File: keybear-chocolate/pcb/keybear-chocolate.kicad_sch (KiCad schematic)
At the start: 95 parts, among them J1 MJ-4PP-9, J2 BATT, J3 LED, J4 OLED, SW1 SW_PUSH, SW10 SW_PUSH, SW11 SW_PUSH, SW12 SW_PUSH, SW13 SW_PUSH, SW14 SW_PUSH, SW15 SW_PUSH, SW16 SW_PUSH, SW17 SW_PUSH, SW18 SW_PUSH, SW19 SW_PUSH, SW2 SW_PUSH, SW20 SW_PUSH, SW21 SW_PUSH, SW22 SW_PUSH, SW23 SW_PUSH, SW25 Rotary_Encoder_Switch, SW3 SW_PUSH, SW30 BATT_SW, SW4 SW_PUSH, SW5 SW_PUSH, SW6 SW_PUSH, SW7 SW_PUSH, SW8 SW_PUSH, SW9 SW_PUSH, U1 ProMicro

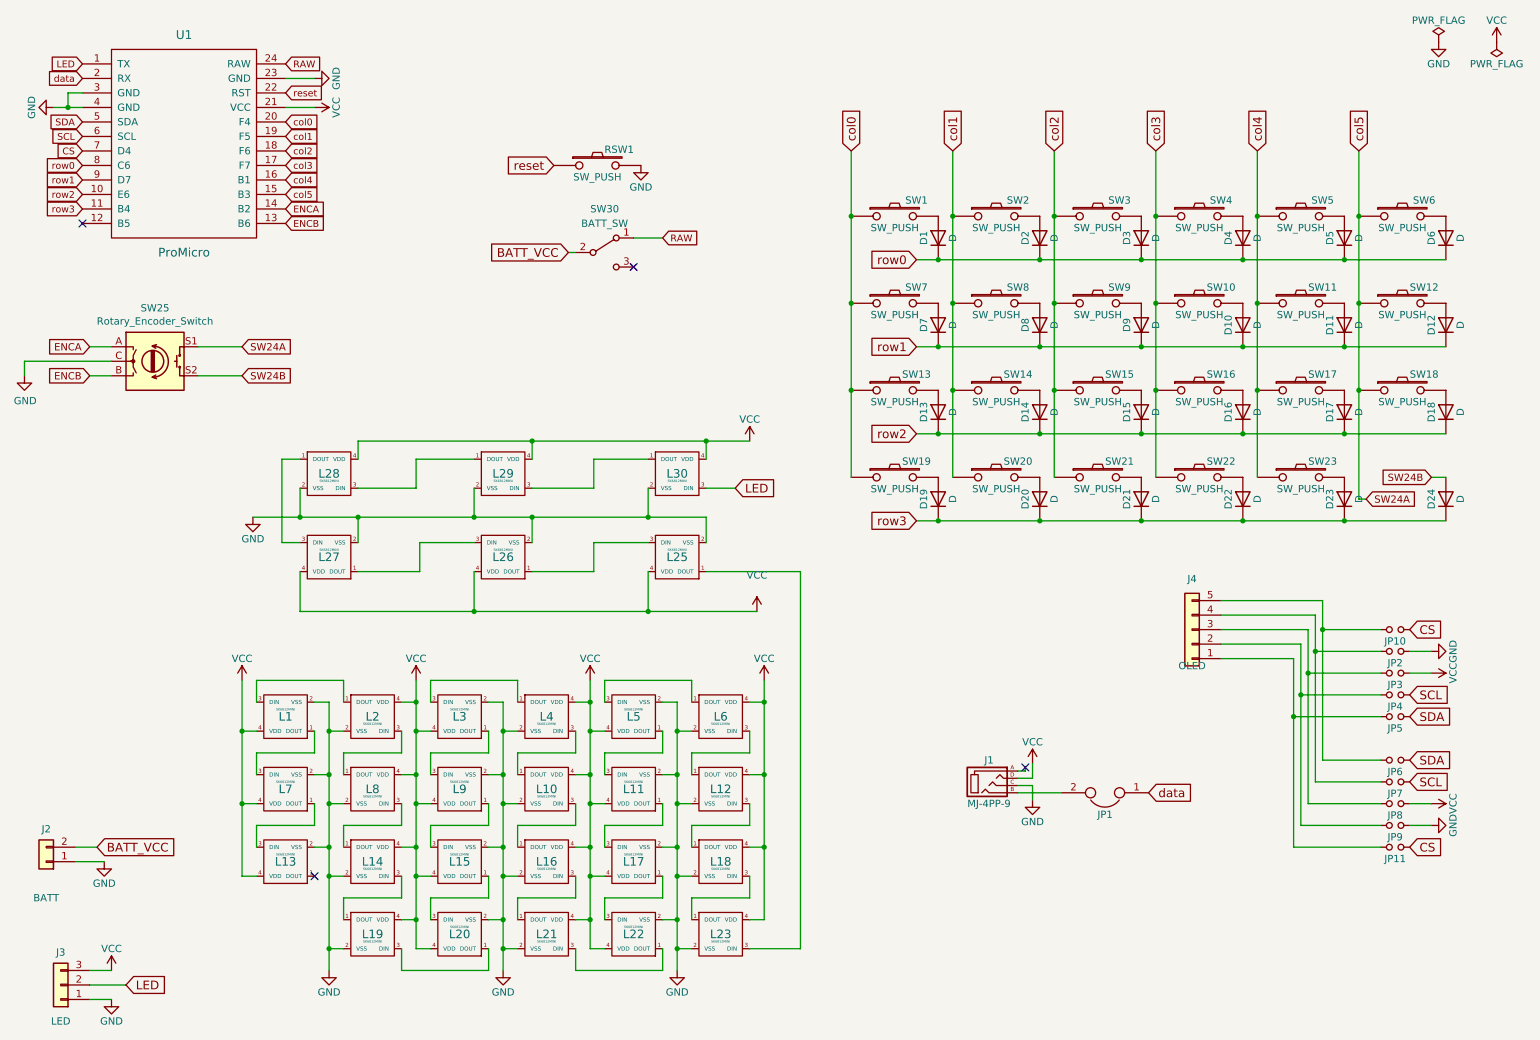
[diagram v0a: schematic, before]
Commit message: batt strip connection updated. tracks made
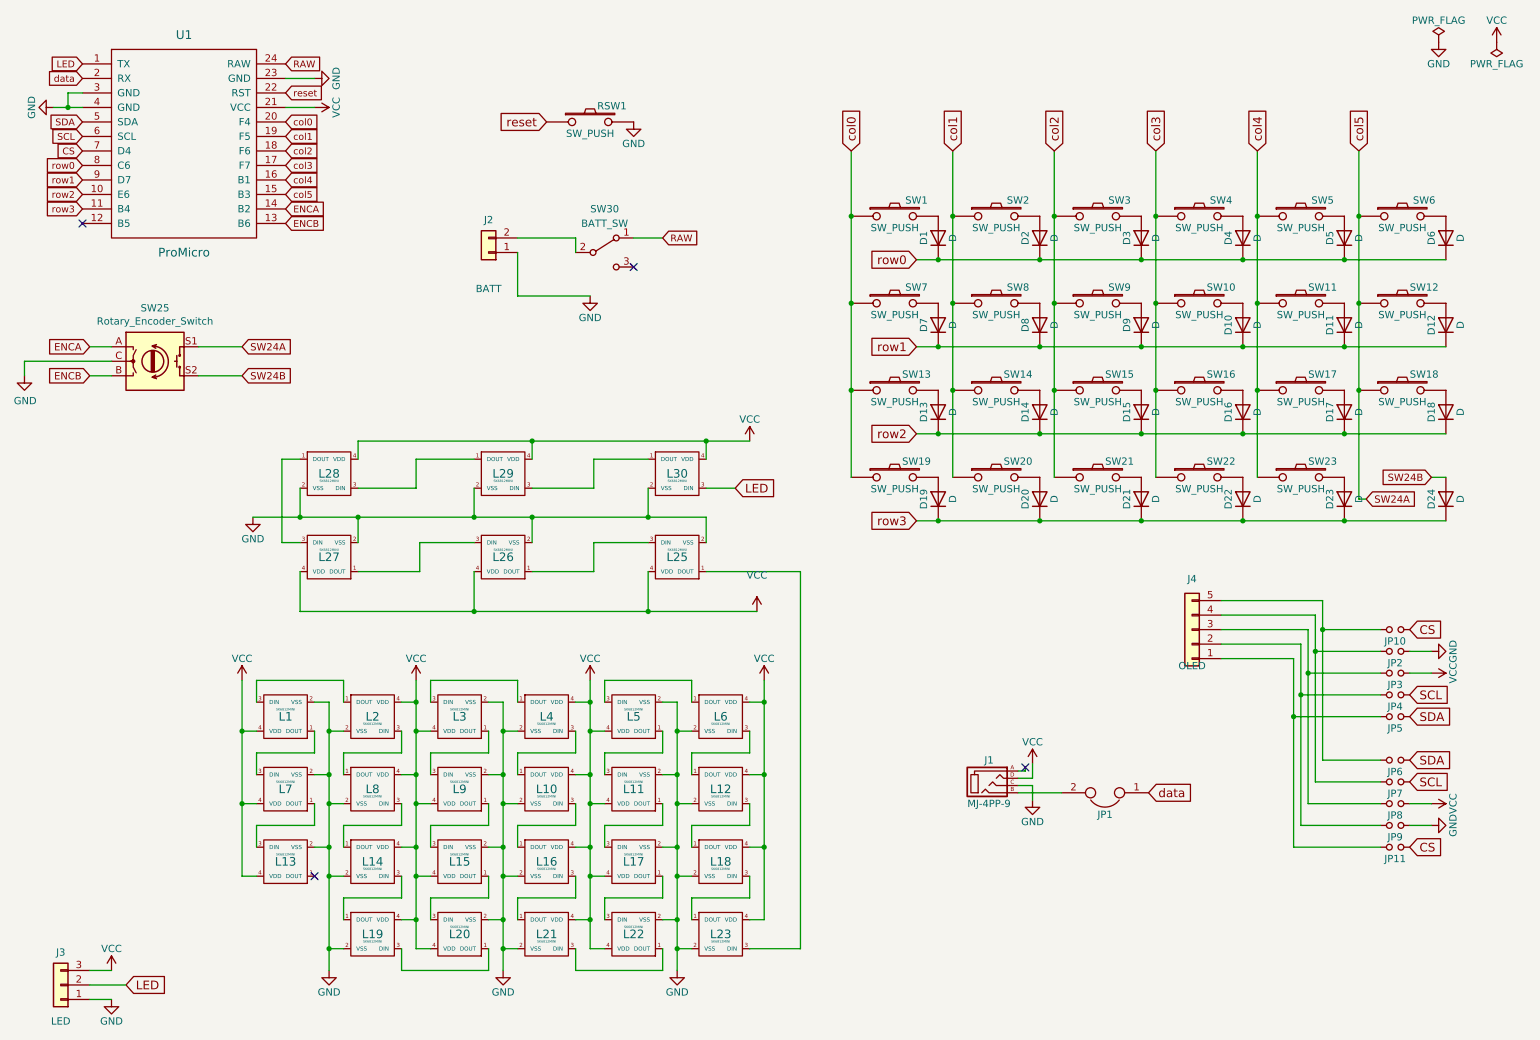
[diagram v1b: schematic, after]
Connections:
- net BATT_VCC: no longer names the net of J2.2 (Pin_2), SW30.2 (B)
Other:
- moved on the sheet: J2, RSW1
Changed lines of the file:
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@@
     (stroke (width 0) (type default))
   )
-  (wire (pts (xy 27.94 163.83) (xy 33.02 163.83))
+  (wire (pts (xy 105.41 54.61) (xy 115.57 54.61))
     (stroke (width 0) (type default))
   )
@@
     (stroke (width 0) (type default))
   )
+  (wire (pts (xy 105.41 64.77) (xy 118.11 64.77))
+    (stroke (width 0) (type default))
+  )
   (wire (pts (xy 115.57 161.29) (xy 118.11 161.29))
     (stroke (width 0) (type default))
@@
     (stroke (width 0) (type default))
   )
+  (wire (pts (xy 115.57 54.61) (xy 115.57 57.15))
+    (stroke (width 0) (type default))
+  )
   (wire (pts (xy 234.95 66.04) (xy 234.95 81.28))
     (stroke (width 0) (type default))
@@
     (stroke (width 0) (type default))
   )
-  (wire (pts (xy 31.75 161.29) (xy 27.94 161.29))
-    (stroke (width 0) (type default))
-  )
   (wire (pts (xy 130.81 179.07) (xy 130.81 182.88))
     (stroke (width 0) (type default))
@@
     (stroke (width 0) (type default))
   )
+  (wire (pts (xy 105.41 57.15) (xy 105.41 64.77))
+    (stroke (width 0) (type default))
+  )
   (wire (pts (xy 146.05 148.59) (xy 148.59 148.59))
     (stroke (width 0) (type default))
@@
     (stroke (width 0) (type default))
   )
-  (wire (pts (xy 115.57 57.15) (xy 114.3 57.15))
-    (stroke (width 0) (type default))
-  )
   (wire (pts (xy 243.84 153.67) (xy 256.54 153.67))
     (stroke (width 0) (type default))
@@
     )
   )
-  (global_label "BATT_VCC" (shape input) (at 114.3 57.15 180) (fields_autoplaced)
-    (effects (font (size 1.524 1.524)) (justify right))
-    (property "Intersheetrefs" "${INTERSHEET_REFS}" (at 100.8353 57.15 0)
-      (effects (font (size 1.27 1.27)) (justify right) hide)
-    )
-  )
   (global_label "SDA" (shape input) (at 261.62 146.05 0) (fields_autoplaced)
     (effects (font (size 1.524 1.524)) (justify left))
@@
     )
   )
-  (global_label "reset" (shape input) (at 111.76 41.91 180) (fields_autoplaced)
+  (global_label "reset" (shape input) (at 110.49 34.29 180) (fields_autoplaced)
     (effects (font (size 1.524 1.524)) (justify right))
-    (property "Intersheetrefs" "${INTERSHEET_REFS}" (at 103.3026 41.91 0)
+    (property "Intersheetrefs" "${INTERSHEET_REFS}" (at 102.0326 34.29 0)
       (effects (font (size 1.27 1.27)) (justify right) hide)
     )
@@
     )
   )
-  (global_label "BATT_VCC" (shape input) (at 31.75 161.29 0) (fields_autoplaced)
-    (effects (font (size 1.524 1.524)) (justify left))
-    (property "Intersheetrefs" "${INTERSHEET_REFS}" (at 45.2147 161.29 0)
-      (effects (font (size 1.27 1.27)) (justify left) hide)
-    )
-  )
   (global_label "col2" (shape input) (at 64.77 39.37 0) (fields_autoplaced)
     (effects (font (size 1.1938 1.1938)) (justify left))
@@
     )
   )
-  (symbol (lib_id "corne-chocolate-rescue:SW_PUSH-kbd") (at 119.38 41.91 0) (unit 1)
+  (symbol (lib_id "corne-chocolate-rescue:SW_PUSH-kbd") (at 118.11 34.29 0) (unit 1)
     (in_bom yes) (on_board yes) (dnp no)
-    (property "Reference" "RSW1" (at 123.19 39.116 0)
+    (property "Reference" "RSW1" (at 121.92 31.496 0)
       (effects (font (size 1.27 1.27)))
     )
-    (property "Value" "SW_PUSH" (at 119.38 43.942 0)
+    (property "Value" "SW_PUSH" (at 118.11 36.322 0)
       (effects (font (size 1.27 1.27)))
     )
-    (property "Footprint" "kbd:ResetSW" (at 119.38 41.91 0)
+    (property "Footprint" "kbd:ResetSW" (at 118.11 34.29 0)
       (effects (font (size 1.27 1.27)) hide)
     )
-    (property "Datasheet" "" (at 119.38 41.91 0)
+    (property "Datasheet" "" (at 118.11 34.29 0)
       (effects (font (size 1.27 1.27)))
     )
@@
     )
   )
-  (symbol (lib_id "power:GND") (at 127 41.91 0) (unit 1)
+  (symbol (lib_id "power:GND") (at 125.73 34.29 0) (unit 1)
     (in_bom yes) (on_board yes) (dnp no)
-    (property "Reference" "#PWR07" (at 127 48.26 0)
+    (property "Reference" "#PWR07" (at 125.73 40.64 0)
       (effects (font (size 1.27 1.27)) hide)
     )
-    (property "Value" "GND" (at 127 45.72 0)
+    (property "Value" "GND" (at 125.73 38.1 0)
       (effects (font (size 1.27 1.27)))
     )
-    (property "Footprint" "" (at 127 41.91 0)
+    (property "Footprint" "" (at 125.73 34.29 0)
       (effects (font (size 1.27 1.27)) hide)
     )
-    (property "Datasheet" "" (at 127 41.91 0)
+    (property "Datasheet" "" (at 125.73 34.29 0)
       (effects (font (size 1.27 1.27)) hide)
     )
@@
     )
   )
-  (symbol (lib_id "power:GND") (at 33.02 163.83 0) (unit 1)
+  (symbol (lib_id "power:GND") (at 118.11 64.77 0) (unit 1)
     (in_bom yes) (on_board yes) (dnp no)
-    (property "Reference" "#PWR021" (at 33.02 170.18 0)
+    (property "Reference" "#PWR021" (at 118.11 71.12 0)
       (effects (font (size 1.27 1.27)) hide)
     )
-    (property "Value" "GND" (at 33.02 167.64 0)
+    (property "Value" "GND" (at 118.11 68.58 0)
       (effects (font (size 1.27 1.27)))
     )
-    (property "Footprint" "" (at 33.02 163.83 0)
+    (property "Footprint" "" (at 118.11 64.77 0)
       (effects (font (size 1.27 1.27)) hide)
     )
-    (property "Datasheet" "" (at 33.02 163.83 0)
+    (property "Datasheet" "" (at 118.11 64.77 0)
       (effects (font (size 1.27 1.27)) hide)
     )
@@
     )
   )
-  (symbol (lib_id "Connector_Generic:Conn_01x02") (at 22.86 163.83 180) (unit 1)
+  (symbol (lib_id "Connector_Generic:Conn_01x02") (at 100.33 57.15 180) (unit 1)
     (in_bom yes) (on_board yes) (dnp no)
-    (property "Reference" "J2" (at 22.86 158.115 0)
+    (property "Reference" "J2" (at 100.33 51.435 0)
       (effects (font (size 1.27 1.27)))
     )
-    (property "Value" "BATT" (at 22.86 170.18 0)
+    (property "Value" "BATT" (at 100.33 63.5 0)
       (effects (font (size 1.27 1.27)))
     )
-    (property "Footprint" "kbd:StripBATT_xo" (at 22.86 163.83 0)
+    (property "Footprint" "kbd:StripBATT_xo" (at 100.33 57.15 0)
       (effects (font (size 1.27 1.27)) hide)
     )
-    (property "Datasheet" "~" (at 22.86 163.83 0)
+    (property "Datasheet" "~" (at 100.33 57.15 0)
       (effects (font (size 1.27 1.27)) hide)
     )

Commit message: LEDs footprint updated an DRC errors fixed
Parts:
- L1, L10, L11, L12, L13, L14, L15, L16, L17, L18, L19, L2, L20, L21, L22, L23, L25, L26, L27, L28, L29, L3, L30, L4, L5, L6, L7, L8, L9: footprint kbd:SK6812MINI_xo_rev -> kbd:SK6812MINI_xo_v02
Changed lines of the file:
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@@
       (effects (font (size 0.4064 0.4064)))
     )
-    (property "Footprint" "kbd:SK6812MINI_xo_rev" (at 80.01 138.43 0)
+    (property "Footprint" "kbd:SK6812MINI_xo_v02" (at 80.01 138.43 0)
       (effects (font (size 1.524 1.524)) hide)
     )
@@
       (effects (font (size 0.4064 0.4064)))
     )
-    (property "Footprint" "kbd:SK6812MINI_xo_rev" (at 95.25 138.43 0)
+    (property "Footprint" "kbd:SK6812MINI_xo_v02" (at 95.25 138.43 0)
       (effects (font (size 1.524 1.524)) hide)
     )
@@
       (effects (font (size 0.4064 0.4064)))
     )
-    (property "Footprint" "kbd:SK6812MINI_xo_rev" (at 110.49 138.43 0)
+    (property "Footprint" "kbd:SK6812MINI_xo_v02" (at 110.49 138.43 0)
       (effects (font (size 1.524 1.524)) hide)
     )
@@
       (effects (font (size 0.4064 0.4064)))
     )
-    (property "Footprint" "kbd:SK6812MINI_xo_rev" (at 125.73 138.43 0)
+    (property "Footprint" "kbd:SK6812MINI_xo_v02" (at 125.73 138.43 0)
       (effects (font (size 1.524 1.524)) hide)
     )
@@
       (effects (font (size 0.4064 0.4064)))
     )
-    (property "Footprint" "kbd:SK6812MINI_xo_rev" (at 140.97 138.43 0)
+    (property "Footprint" "kbd:SK6812MINI_xo_v02" (at 140.97 138.43 0)
       (effects (font (size 1.524 1.524)) hide)
     )
@@
       (effects (font (size 0.4064 0.4064)))
     )
-    (property "Footprint" "kbd:SK6812MINI_xo_rev" (at 64.77 138.43 0)
+    (property "Footprint" "kbd:SK6812MINI_xo_v02" (at 64.77 138.43 0)
       (effects (font (size 1.524 1.524)) hide)
     )
@@
       (effects (font (size 0.4064 0.4064)))
     )
-    (property "Footprint" "kbd:SK6812MINI_xo_rev" (at 80.01 151.13 0)
+    (property "Footprint" "kbd:SK6812MINI_xo_v02" (at 80.01 151.13 0)
       (effects (font (size 1.524 1.524)) hide)
     )
@@
       (effects (font (size 0.4064 0.4064)))
     )
-    (property "Footprint" "kbd:SK6812MINI_xo_rev" (at 95.25 151.13 0)
+    (property "Footprint" "kbd:SK6812MINI_xo_v02" (at 95.25 151.13 0)
       (effects (font (size 1.524 1.524)) hide)
     )
@@
       (effects (font (size 0.4064 0.4064)))
     )
-    (property "Footprint" "kbd:SK6812MINI_xo_rev" (at 110.49 151.13 0)
+    (property "Footprint" "kbd:SK6812MINI_xo_v02" (at 110.49 151.13 0)
       (effects (font (size 1.524 1.524)) hide)
     )
@@
       (effects (font (size 0.4064 0.4064)))
     )
-    (property "Footprint" "kbd:SK6812MINI_xo_rev" (at 125.73 151.13 0)
+    (property "Footprint" "kbd:SK6812MINI_xo_v02" (at 125.73 151.13 0)
       (effects (font (size 1.524 1.524)) hide)
     )
@@
       (effects (font (size 0.4064 0.4064)))
     )
-    (property "Footprint" "kbd:SK6812MINI_xo_rev" (at 140.97 151.13 0)
+    (property "Footprint" "kbd:SK6812MINI_xo_v02" (at 140.97 151.13 0)
       (effects (font (size 1.524 1.524)) hide)
     )
@@
       (effects (font (size 0.4064 0.4064)))
     )
-    (property "Footprint" "kbd:SK6812MINI_xo_rev" (at 64.77 151.13 0)
+    (property "Footprint" "kbd:SK6812MINI_xo_v02" (at 64.77 151.13 0)
       (effects (font (size 1.524 1.524)) hide)
     )
@@
       (effects (font (size 0.4064 0.4064)))
     )
-    (property "Footprint" "kbd:SK6812MINI_xo_rev" (at 80.01 163.83 0)
+    (property "Footprint" "kbd:SK6812MINI_xo_v02" (at 80.01 163.83 0)
       (effects (font (size 1.524 1.524)) hide)
     )
@@
       (effects (font (size 0.4064 0.4064)))
     )
-    (property "Footprint" "kbd:SK6812MINI_xo_rev" (at 95.25 163.83 0)
+    (property "Footprint" "kbd:SK6812MINI_xo_v02" (at 95.25 163.83 0)
       (effects (font (size 1.524 1.524)) hide)
     )
@@
       (effects (font (size 0.4064 0.4064)))
     )
-    (property "Footprint" "kbd:SK6812MINI_xo_rev" (at 110.49 163.83 0)
+    (property "Footprint" "kbd:SK6812MINI_xo_v02" (at 110.49 163.83 0)
       (effects (font (size 1.524 1.524)) hide)
     )
@@
       (effects (font (size 0.4064 0.4064)))
     )
-    (property "Footprint" "kbd:SK6812MINI_xo_rev" (at 125.73 163.83 0)
+    (property "Footprint" "kbd:SK6812MINI_xo_v02" (at 125.73 163.83 0)
       (effects (font (size 1.524 1.524)) hide)
     )
@@
       (effects (font (size 0.4064 0.4064)))
     )
-    (property "Footprint" "kbd:SK6812MINI_xo_rev" (at 140.97 163.83 0)
+    (property "Footprint" "kbd:SK6812MINI_xo_v02" (at 140.97 163.83 0)
       (effects (font (size 1.524 1.524)) hide)
     )
@@
       (effects (font (size 0.4064 0.4064)))
     )
-    (property "Footprint" "kbd:SK6812MINI_xo_rev" (at 64.77 163.83 0)
+    (property "Footprint" "kbd:SK6812MINI_xo_v02" (at 64.77 163.83 0)
       (effects (font (size 1.524 1.524)) hide)
     )
@@
       (effects (font (size 0.4064 0.4064)))
     )
-    (property "Footprint" "kbd:SK6812MINI_xo_rev" (at 125.73 176.53 0)
+    (property "Footprint" "kbd:SK6812MINI_xo_v02" (at 125.73 176.53 0)
       (effects (font (size 1.524 1.524)) hide)
     )
@@
       (effects (font (size 0.4064 0.4064)))
     )
-    (property "Footprint" "kbd:SK6812MINI_xo_rev" (at 140.97 176.53 0)
+    (property "Footprint" "kbd:SK6812MINI_xo_v02" (at 140.97 176.53 0)
       (effects (font (size 1.524 1.524)) hide)
     )
@@
       (effects (font (size 0.4064 0.4064)))
     )
-    (property "Footprint" "kbd:SK6812MINI_xo_rev" (at 110.49 176.53 0)
+    (property "Footprint" "kbd:SK6812MINI_xo_v02" (at 110.49 176.53 0)
       (effects (font (size 1.524 1.524)) hide)
     )
@@
       (effects (font (size 0.4064 0.4064)))
     )
-    (property "Footprint" "kbd:SK6812MINI_xo_rev" (at 133.35 95.885 0)
+    (property "Footprint" "kbd:SK6812MINI_xo_v02" (at 133.35 95.885 0)
       (effects (font (size 1.524 1.524)) hide)
     )
@@
       (effects (font (size 0.4064 0.4064)))
     )
-    (property "Footprint" "kbd:SK6812MINI_xo_rev" (at 102.87 95.885 0)
+    (property "Footprint" "kbd:SK6812MINI_xo_v02" (at 102.87 95.885 0)
       (effects (font (size 1.524 1.524)) hide)
     )
@@
       (effects (font (size 0.4064 0.4064)))
     )
-    (property "Footprint" "kbd:SK6812MINI_xo_rev" (at 72.39 95.885 0)
+    (property "Footprint" "kbd:SK6812MINI_xo_v02" (at 72.39 95.885 0)
       (effects (font (size 1.524 1.524)) hide)
     )
@@
       (effects (font (size 0.4064 0.4064)))
     )
-    (property "Footprint" "kbd:SK6812MINI_xo_rev" (at 133.35 110.49 0)
+    (property "Footprint" "kbd:SK6812MINI_xo_v02" (at 133.35 110.49 0)
       (effects (font (size 1.524 1.524)) hide)
     )
@@
       (effects (font (size 0.4064 0.4064)))
     )
-    (property "Footprint" "kbd:SK6812MINI_xo_rev" (at 102.87 110.49 0)
+    (property "Footprint" "kbd:SK6812MINI_xo_v02" (at 102.87 110.49 0)
       (effects (font (size 1.524 1.524)) hide)
     )
@@
       (effects (font (size 0.4064 0.4064)))
     )
-    (property "Footprint" "kbd:SK6812MINI_xo_rev" (at 72.39 110.49 0)
+    (property "Footprint" "kbd:SK6812MINI_xo_v02" (at 72.39 110.49 0)
       (effects (font (size 1.524 1.524)) hide)
     )
@@
       (effects (font (size 0.4064 0.4064)))
     )
-    (property "Footprint" "kbd:SK6812MINI_xo_rev" (at 80.01 176.53 0)
+    (property "Footprint" "kbd:SK6812MINI_xo_v02" (at 80.01 176.53 0)
       (effects (font (size 1.524 1.524)) hide)
     )
@@
       (effects (font (size 0.4064 0.4064)))
     )
-    (property "Footprint" "kbd:SK6812MINI_xo_rev" (at 95.25 176.53 0)
-      (effects (font (size 1.524 1.524)) hide)
-    )
+    (property "Footprint" "kbd:SK6812MINI_xo_v02" (at 95.25 176.53 0)
+      (effects (font (size 1.524 1.524)) hide)
+    )
